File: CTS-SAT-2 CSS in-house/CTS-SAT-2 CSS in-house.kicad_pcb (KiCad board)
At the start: 2 copper layers, 56 parts, among them J1 Conn_01x05_Socket, J12 Socket_1x2, J13 Socket_1x2, J18 Socket_1x2, J19 Socket_1x2, U1 POPA4383PWR, U2 POPA4383PWR, U3 ADS7128IRTET

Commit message: More pcb editing
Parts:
- moved LED6 35.3 mm to (130.6, 74.4), turned to 0 degrees
- moved LED1 21.6 mm to (152.4, 73.2)
- moved C6 20.9 mm to (127.3, 76.0), turned to -90 degrees
- moved R6 19.8 mm to (126.6, 80.3), turned to 180 degrees
- moved C7 18.7 mm to (125.7, 76.1), turned to 90 degrees
- moved R11 18.6 mm to (126.3, 78.5)
- moved U2 13.5 mm to (120.1, 81.2), turned to -90 degrees
- moved C8 13.4 mm to (127.4, 86.5), turned to -90 degrees
- moved R12 12.8 mm to (126.6, 82.0), turned to 0 degrees
- moved R8 12.7 mm to (126.8, 83.8)
- moved C11 12.7 mm to (125.9, 86.5), turned to 90 degrees
- moved LED2 7.11 mm to (130.7, 83.6)
- moved LED5 5.85 mm to (130.6, 76.7)
- moved J13 4.38 mm to (171.2, 73.2)
- moved LED7 1.53 mm to (130.7, 88.1)
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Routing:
- net /ARRAY_SIGNAL_4: track 46.8 -> 13.9 mm
- net /TIA_OUTPUT_6: track 38.9 -> 24.1 mm
- net /ARRAY_SIGNAL_6: track 26.4 -> 13.6 mm
- net /1.65V_VGND_1: track 0.00 -> 9.73 mm
- net /TIA_OUTPUT_4: track 33.4 -> 25.9 mm
- net Net-(R12-Pad2): track 7.94 -> 2.64 mm
- net Net-(R11-Pad1): track 8.14 -> 2.89 mm
- net Net-(U2-V+): track 0.00 -> 1.54 mm, vias 0 -> 1

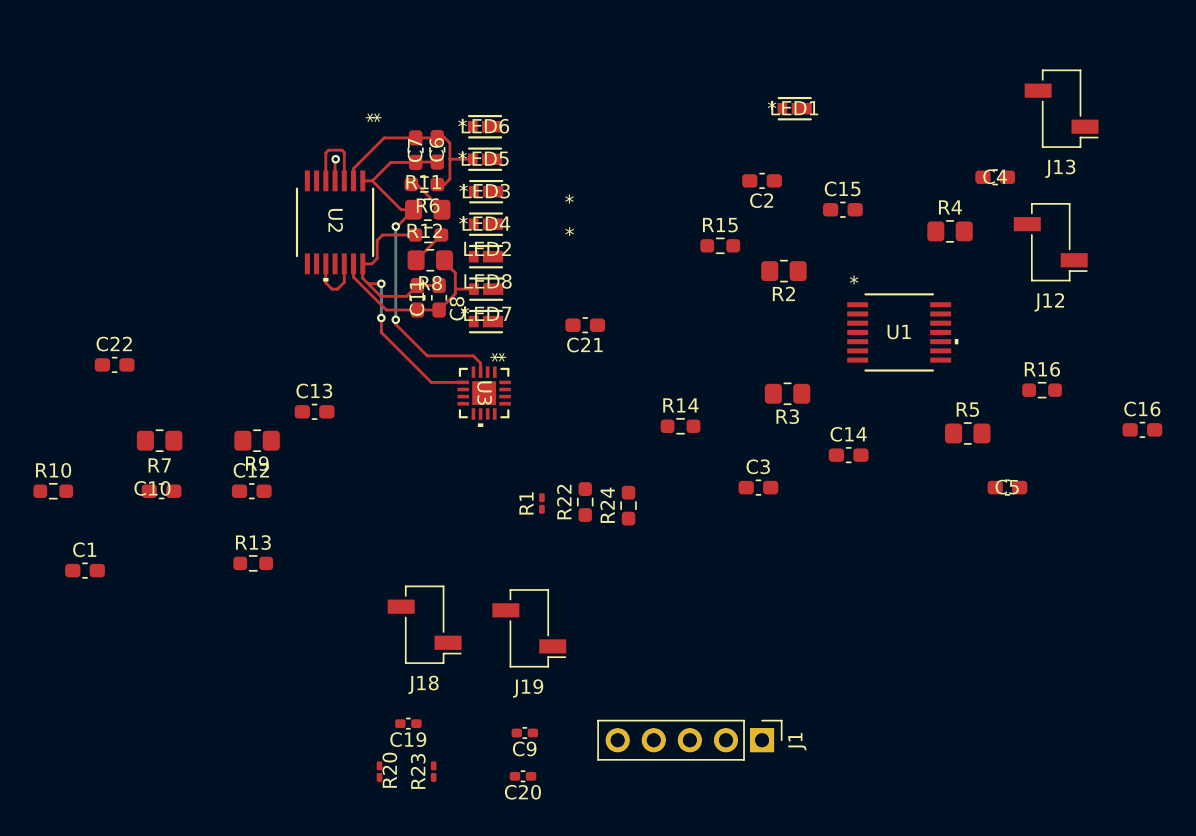
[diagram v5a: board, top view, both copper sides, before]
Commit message: PCB routing first draft
Generally routed the pcb, still drc errors and other things need fixing
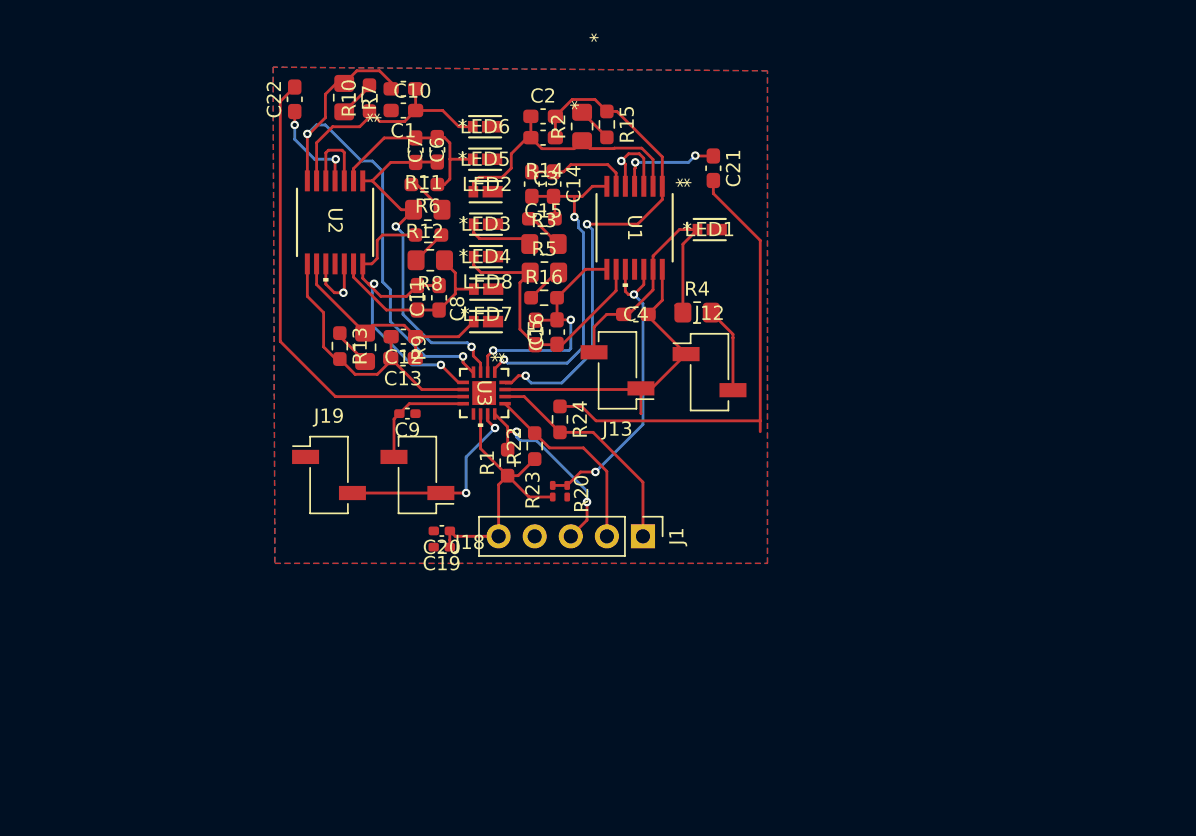
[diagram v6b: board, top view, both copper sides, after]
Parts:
- R1: footprint Resistor_SMD:R_0201_0603Metric_Pad0.64x0.40mm_HandSolder -> Resistor_SMD:R_0603_1608Metric_Pad0.98x0.95mm_HandSolder
- moved C16 41.8 mm to (135.7, 88.9), turned to 90 degrees
- moved C1 39.4 mm to (124.9, 73.3), turned to 180 degrees
- moved J13 36.3 mm to (139.9, 91.6)
- moved R16 35.7 mm to (134.8, 86.5)
- moved R10 35.5 mm to (122.5, 72.4), turned to 90 degrees
- moved C5 35.0 mm to (134.2, 88.9), turned to 90 degrees
- moved C10 33.0 mm to (124.9, 71.8), turned to 180 degrees
- moved R5 31.9 mm to (134.8, 84.7)
- moved C14 28.2 mm to (135.4, 78.5), turned to -90 degrees
- moved R7 27.4 mm to (120.7, 72.4), turned to 90 degrees
- moved C4 27.1 mm to (141.2, 87.6)
- moved C3 26.7 mm to (133.9, 78.5), turned to -90 degrees
- moved J12 25.7 mm to (146.4, 91.7), turned to 0 degrees
- moved C9 23.9 mm to (125.2, 94.6)
- moved R20 23.7 mm to (136.4, 100.1), turned to 90 degrees
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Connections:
- U3 pad 15: /COARSE_TIA_OUTPUT -> /COURSE_TIA_OUTPUT
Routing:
- net /3V3_SUPPLY_1: track 0.00 -> 87.0 mm
- net /TIA_OUTPUT_5: track 0.00 -> 38.5 mm, vias 0 -> 2
- net /TIA_OUPTUT_1: track 0.00 -> 36.9 mm, vias 0 -> 2
- net /1.65V_VGND_1: track 9.73 -> 38.2 mm, vias 0 -> 4
- net /TIA_OUTPUT_2: track 0.00 -> 25.4 mm, vias 0 -> 2
- net /COURSE_TIA_OUTPUT: track 0.00 -> 23.0 mm
- net Net-(J13-Pin_2): track 0.00 -> 20.3 mm
- net /TIA_OUTPUT_7: track 0.00 -> 20.0 mm
- net /ARRAY_SIGNAL_1: track 0.00 -> 19.7 mm
- net /ARRAY_SIGNAL_3: track 0.00 -> 19.4 mm
- net /TIA_OUTPUT_3: track 0.00 -> 17.6 mm, vias 0 -> 2
- net /ARRAY_SIGNAL_5: track 0.00 -> 17.5 mm
- net /ARRAY_SIGNAL_7: track 0.00 -> 16.8 mm
- net Net-(J1-Pin_1): track 0.00 -> 15.5 mm
- net Net-(J18-Pin_1): track 0.00 -> 14.6 mm, vias 0 -> 2
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- added copper zone on B.Cu, net GND
- added copper zone on F.Cu, net GND

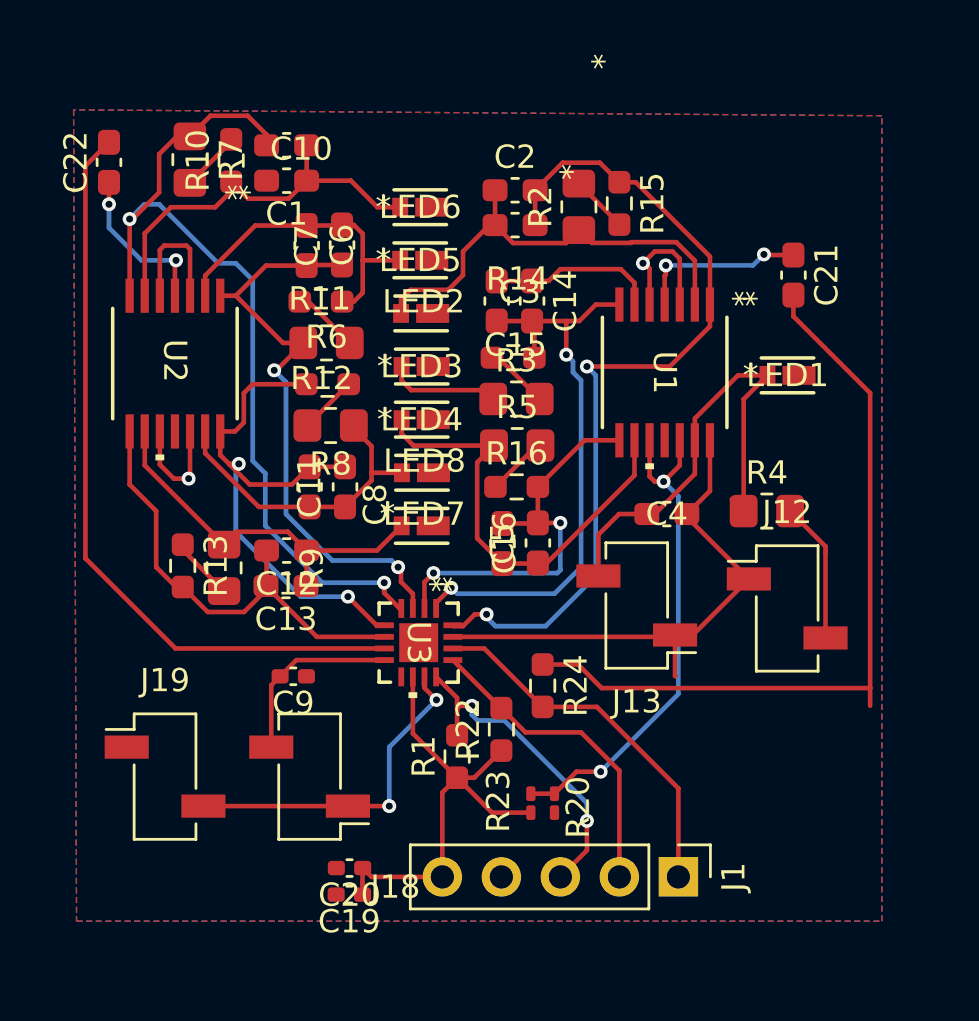
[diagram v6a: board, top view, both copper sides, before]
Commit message: Managing signal integrity
Add ground pours, stitching vias, still need alot to fix.
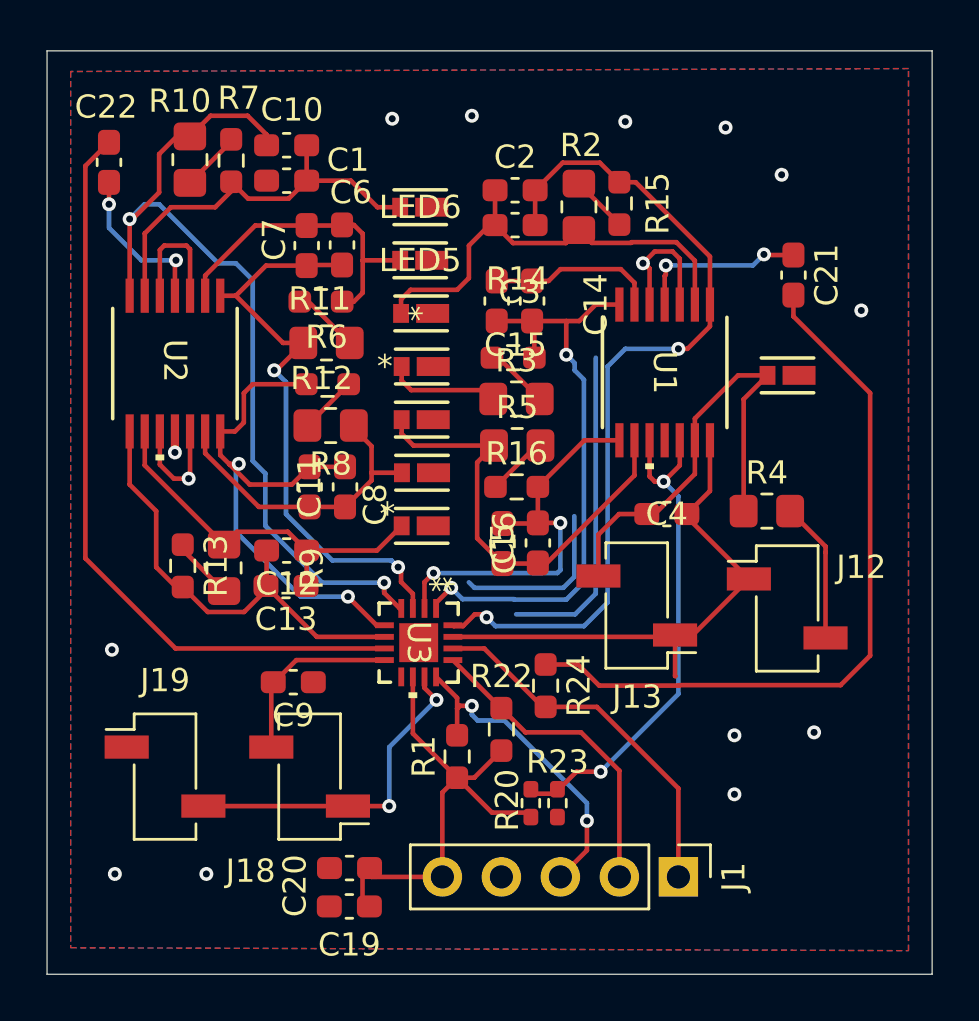
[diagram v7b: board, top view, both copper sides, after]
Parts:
- C19, C20, C9: footprint Capacitor_SMD:C_0402_1005Metric_Pad0.74x0.62mm_HandSolder -> Capacitor_SMD:C_0603_1608Metric_Pad1.08x0.95mm_HandSolder
- R20, R23: footprint Resistor_SMD:R_0201_0603Metric_Pad0.64x0.40mm_HandSolder -> Resistor_SMD:R_0402_1005Metric_Pad0.72x0.64mm_HandSolder
- moved C19 0.51 mm to (127.6, 104.5)
- moved C9 0.25 mm to (125.2, 94.9)
- moved R20 0.13 mm to (136.5, 100.1)
- moved R24 0.13 mm to (136.0, 95.0)
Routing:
- net GND: track 0.00 -> 21.4 mm, vias 0 -> 13
- net /3V3_SUPPLY_1: track 87.0 -> 85.9 mm
- net /TIA_OUTPUT_2: track 25.4 -> 26.1 mm
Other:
- board outline added: 38.1 x 39.8 mm

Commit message: Small changes
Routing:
- net /1.65V_VGND_1: track 38.2 -> 95.5 mm, vias 4 -> 6
- net /3V3_SUPPLY_1: track 85.9 -> 104.1 mm, vias 0 -> 4
- net GND: track 21.4 -> 33.2 mm, vias 13 -> 20
- net /ARRAY_SIGNAL_2: track 12.2 -> 18.0 mm
- net Net-(U2-V+): track 6.96 -> 7.62 mm
